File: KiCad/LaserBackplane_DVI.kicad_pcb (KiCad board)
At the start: 2 copper layers, 69 x 28 mm, 47 parts, among them J1 Curr. Mod., J2 DVI-I, J5 Pz+, J6 Pz-, J7 Piezo_In, J8 Conn_Coaxial, K1 G6AU, Q1 MMBT3904, Q2 2N4401, U1 ADA4807-2ARM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

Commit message: Fix/version (#19)
* Fixed incorrect version label

* Refilled zones

* Updated images
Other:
- board text added: "Rev. 1.8.1"
- board text removed: "Rev. 1.8.0"

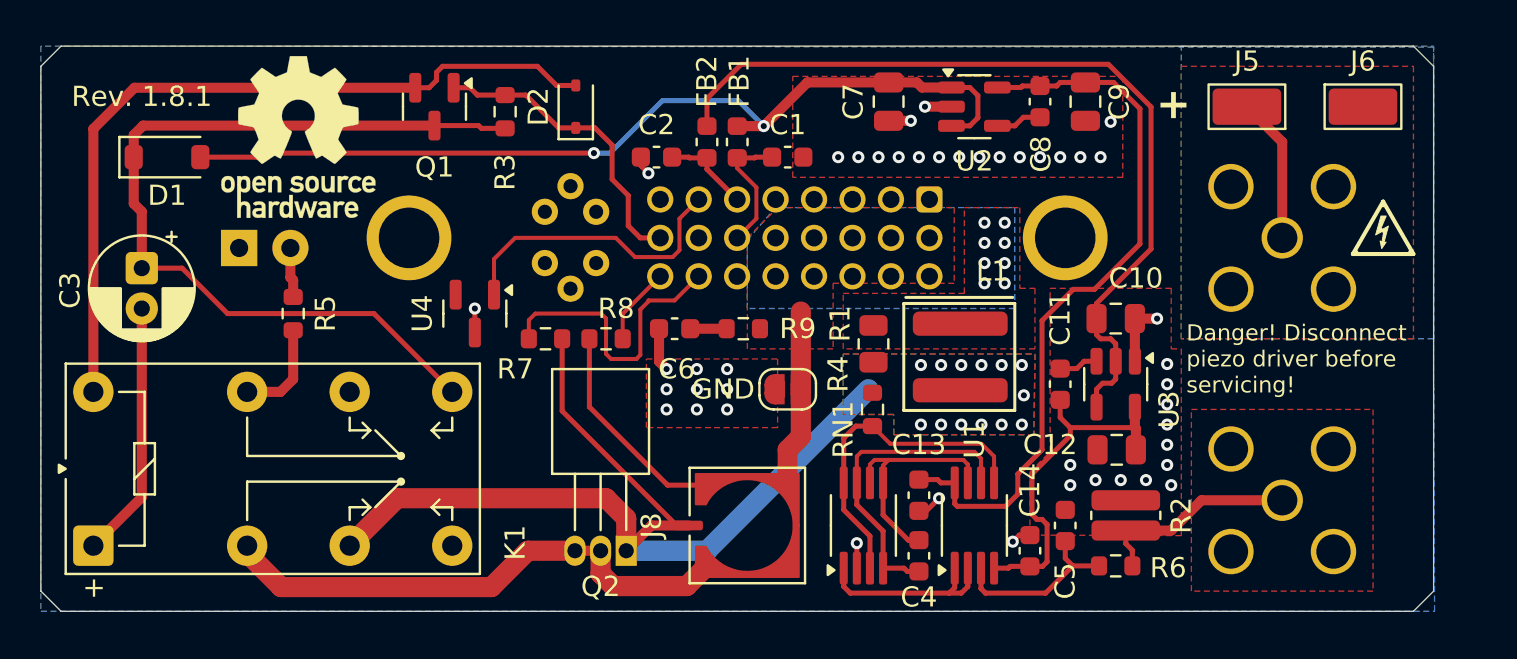
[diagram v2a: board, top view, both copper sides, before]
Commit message: Fixed alignment issues
- Moved the LED D4 up by 0.5 mm to match the DVI connector y position
- Moved the DVI connector 0.005 mm to the right to center it on the PCB
- Updated DVI footprint to center it on pin 14
- Redrawn draces connecting the DVI connector
- Moved piezo labels slight down and away from the edge
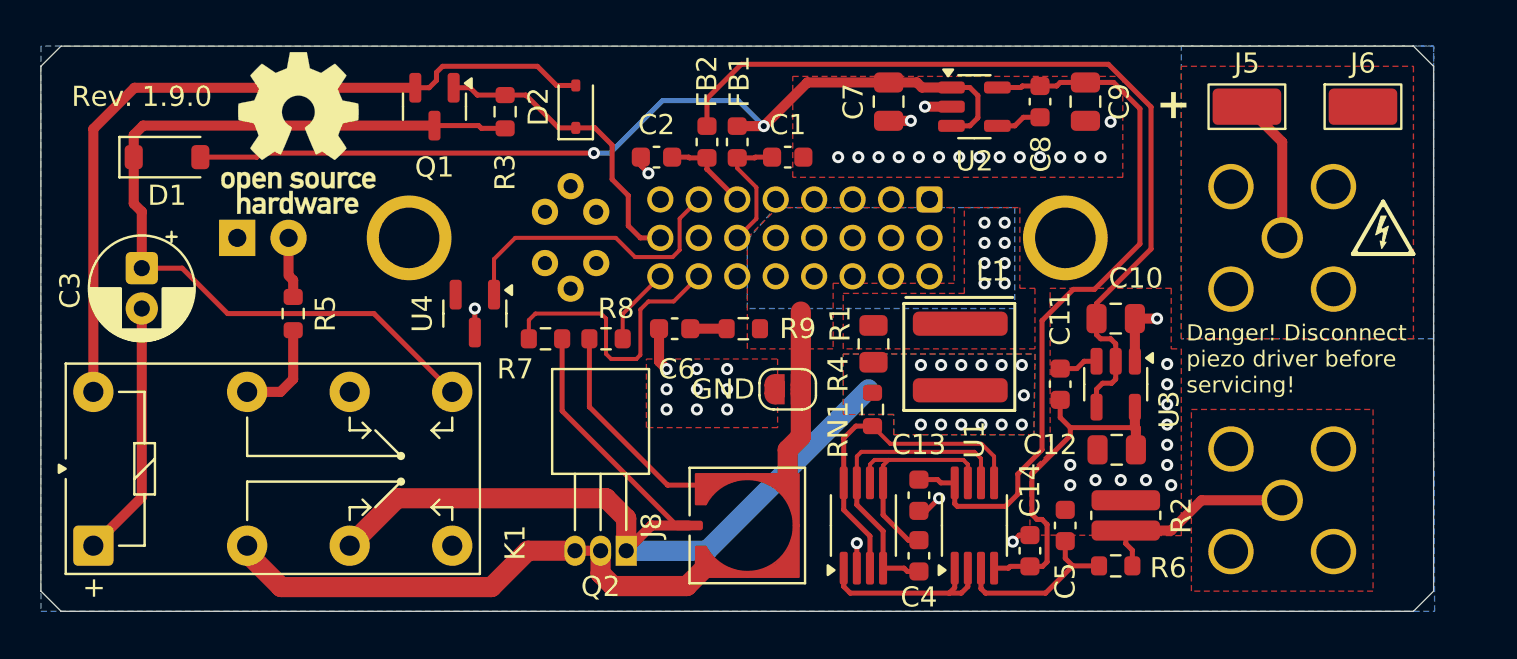
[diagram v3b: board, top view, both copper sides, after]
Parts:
- moved J2 10.7 mm to (124.5, 99.5)
- moved D4 0.51 mm to (99.7, 99.5)
- moved LOGO2 0.20 mm to (102.8, 94.3)
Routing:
- net Net-(J5-Pin_1): track 7.22 -> 2.47 mm
- net Net-(D4-A): track 2.48 -> 3.02 mm
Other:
- board text added: "LaserBackplane v1.9.0 Design: T. Preuschoff, P. Baus Date: 2025-08 https://github.com/TU-Darmstadt-APQ/ Laser_Backplane_DVI"
- board text added: "Rev. 1.9.0"
- board text removed: "LaserBackplane v1.8.1 Design: T. Preuschoff, P. Baus Date: 2025-06 https://github.com/TU-Darmstadt-APQ/ Laser_Backplane_DVI"
- board text removed: "Rev. 1.8.1"
